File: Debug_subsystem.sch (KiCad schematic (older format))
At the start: 2 parts

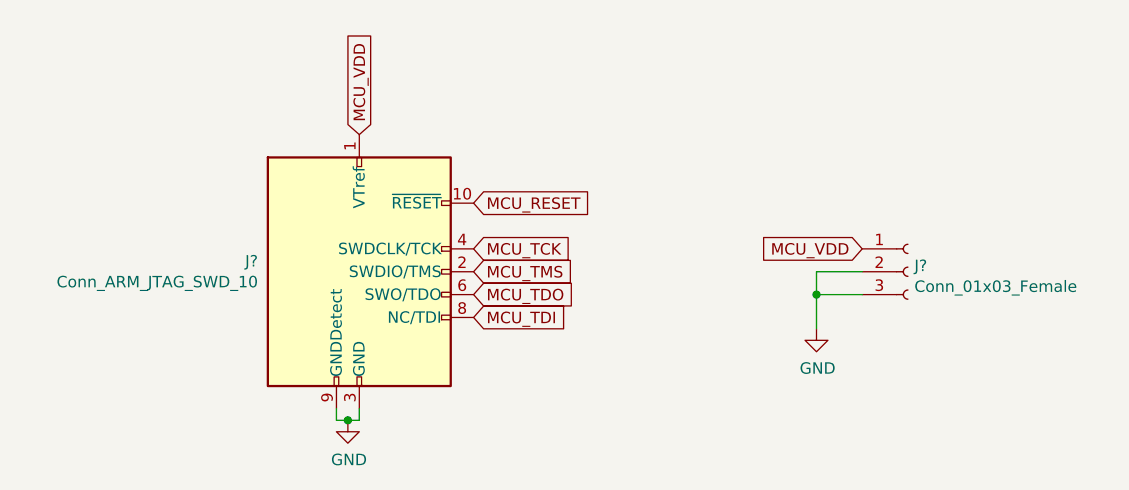
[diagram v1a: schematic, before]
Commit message: Finished Adding MCU connections and combined crystal and MCU sheets.
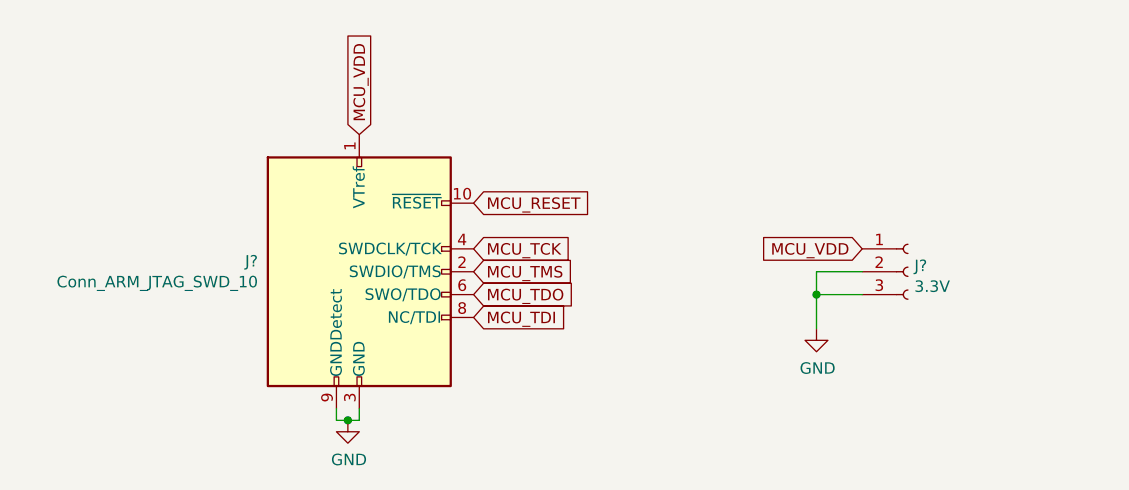
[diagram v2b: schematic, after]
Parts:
- J?: value Conn_01x03_Female -> 3.3V
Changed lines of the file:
@@
 $Descr A4 11693 8268
 encoding utf-8
-Sheet 6 7
+Sheet 5 6
 Title ""
 Date ""
@@
 P 7550 3550
 F 0 "J?" H 7578 3576 50  0000 L CNN
-F 1 "Conn_01x03_Female" H 7578 3485 50  0000 L CNN
+F 1 "3.3V" H 7578 3485 50  0000 L CNN
 F 2 "" H 7550 3550 50  0001 C CNN
 F 3 "~" H 7550 3550 50  0001 C CNN

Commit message: part way through PCB rework using new components. 62 unconnected.
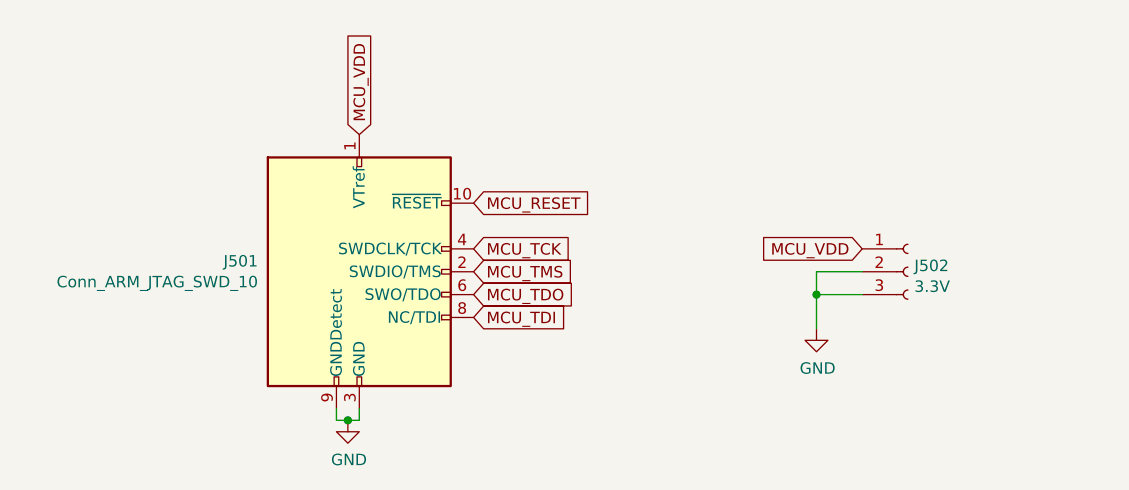
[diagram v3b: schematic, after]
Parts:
- gave numbers to parts that had none: 2
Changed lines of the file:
@@
 $EndDescr
 $Comp
-L Connector:Conn_ARM_JTAG_SWD_10 J?
+L Connector:Conn_ARM_JTAG_SWD_10 J501
 U 1 1 614AA0C1
 P 5150 3550
-F 0 "J?" H 4707 3596 50  0000 R CNN
+F 0 "J501" H 4707 3596 50  0000 R CNN
 F 1 "Conn_ARM_JTAG_SWD_10" H 4707 3505 50  0000 R CNN
 F 2 "" H 5150 3550 50  0001 C CNN
@@
 MCU_RESET
 $Comp
-L power:GND #PWR?
+L power:GND #PWR0501
 U 1 1 614AB0A8
 P 5100 4200
-F 0 "#PWR?" H 5100 3950 50  0001 C CNN
+F 0 "#PWR0501" H 5100 3950 50  0001 C CNN
 F 1 "GND" H 5105 4027 50  0000 C CNN
 F 2 "" H 5100 4200 50  0001 C CNN
@@
 MCU_VDD
 $Comp
-L Connector:Conn_01x03_Female J?
+L Connector:Conn_01x03_Female J502
 U 1 1 614ABF85
 P 7550 3550
-F 0 "J?" H 7578 3576 50  0000 L CNN
+F 0 "J502" H 7578 3576 50  0000 L CNN
 F 1 "3.3V" H 7578 3485 50  0000 L CNN
 F 2 "" H 7550 3550 50  0001 C CNN
@@
 MCU_VDD
 $Comp
-L power:GND #PWR?
+L power:GND #PWR0502
 U 1 1 614AC7F9
 P 7150 3800
-F 0 "#PWR?" H 7150 3550 50  0001 C CNN
+F 0 "#PWR0502" H 7150 3550 50  0001 C CNN
 F 1 "GND" H 7155 3627 50  0000 C CNN
 F 2 "" H 7150 3800 50  0001 C CNN
